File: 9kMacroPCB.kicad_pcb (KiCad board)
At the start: 2 copper layers, 60.3 x 60.3 mm, 25 parts, among them U1 XIAO-RP2040-SMD

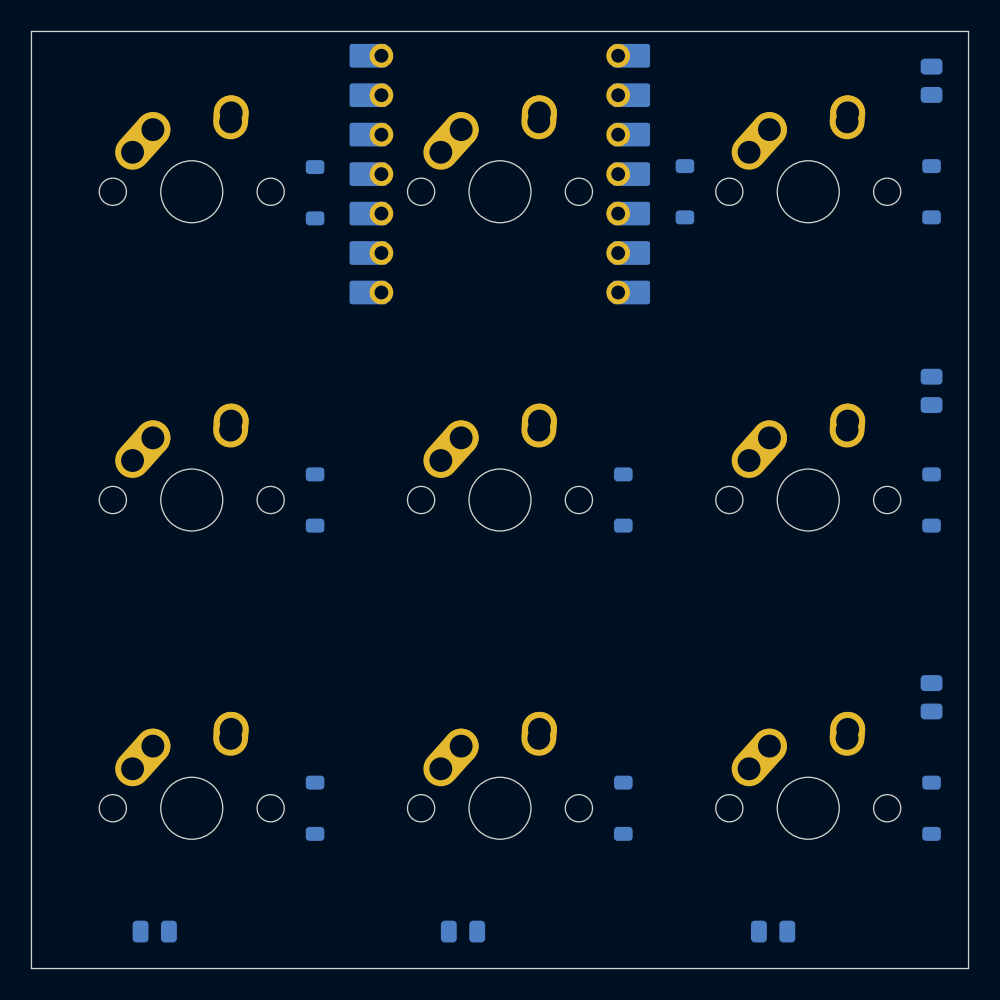
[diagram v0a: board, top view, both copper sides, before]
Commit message: Update PCB: netlist, footprints, and backup cleanup
Removed old backup zip files and added an auto-saved file reference. Updated net assignments and pin naming in 9kMacroPCB.kicad_pcb, made significant changes to footprints (notably D1, R4, and U1), and adjusted component placements and net connections. These changes reflect schematic and layout updates for improved accuracy and maintainability.
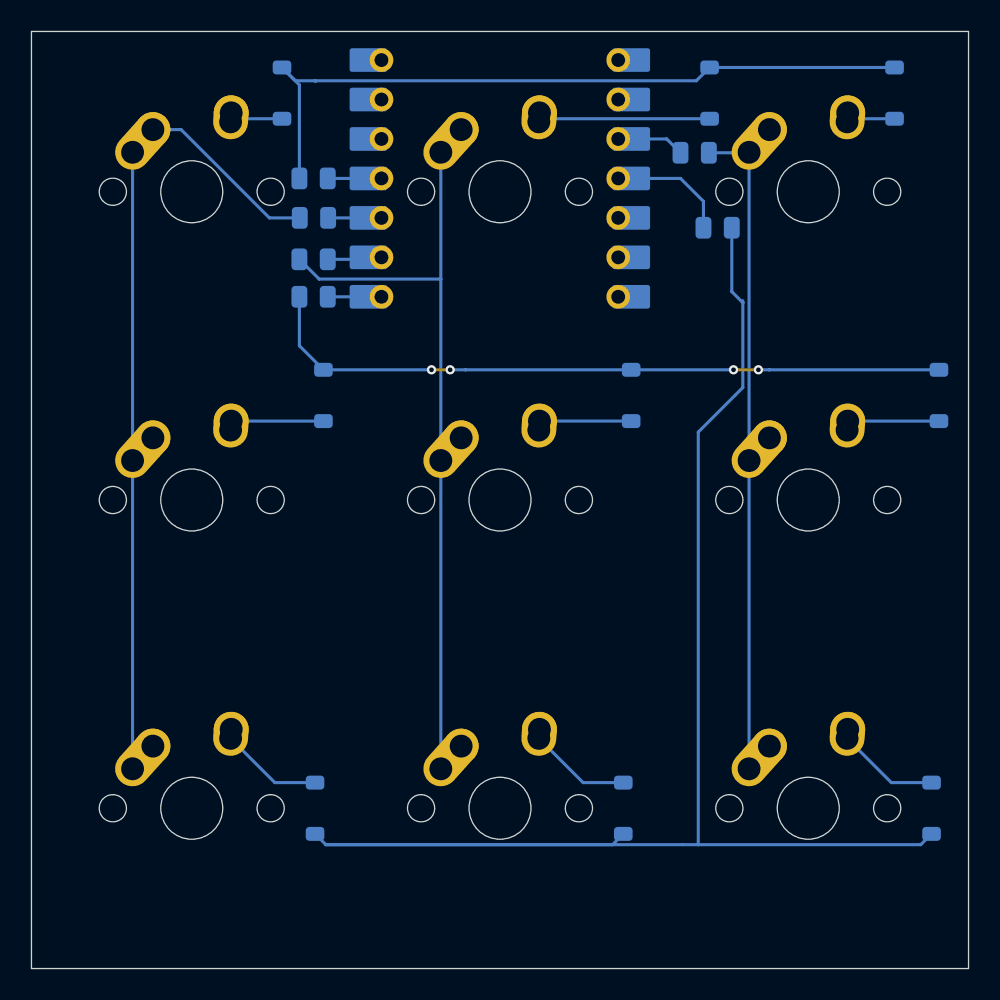
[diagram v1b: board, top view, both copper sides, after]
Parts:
- R1, R2, R3, R4, R5, R6: value 10k -> R_Small
- U1: value XIAO-RP2040-SMD -> XIAO-RP2040-DIP; footprint Seeed Studio XIAO Series Library:XIAO-RP2040-DIP -> XIAO_PCB:XIAO-RP2040-DIP
- moved R5 52.3 mm to (157.0, 47.5)
- moved R3 47.4 mm to (132.5, 56.8), turned to 180 degrees
- moved R6 45.4 mm to (158.5, 52.3)
- moved R4 44.5 mm to (132.5, 54.4)
- moved R2 41.3 mm to (132.5, 51.7), turned to 180 degrees
- moved R1 40.3 mm to (132.5, 49.1), turned to 180 degrees
- moved D3 6.78 mm to (169.9, 43.7), turned to -90 degrees
- moved D1 6.76 mm to (130.4, 43.7), turned to -90 degrees
- moved D4 6.75 mm to (133.1, 63.1), turned to -90 degrees
- moved D5 6.75 mm to (152.9, 63.1), turned to -90 degrees
- moved D6 6.75 mm to (172.7, 63.1), turned to -90 degrees
- moved D2 6.55 mm to (158.0, 43.7), turned to -90 degrees
- moved U1 0.28 mm to (144.5, 49.1)
- renumbered D6 to D2, D7 to D3, D2 to D4, D8 to D6, D3 to D7, D4 to D8
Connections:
- R1 pad 1: unconnected-(R1-Pad1) -> Net-(U1-GPIO3/MOSI)
- R1 pad 2: Net-(U1-GPIO26_A0_D0) -> ROW0
- R2 pad 1: unconnected-(R2-Pad1) -> Net-(U1-GPIO4/MISO)
- R2 pad 2: Net-(U1-GPIO27_A1_D1) -> COL0
- R3 pad 1: unconnected-(R3-Pad1) -> Net-(U1-GPIO1/RX)
- R3 pad 2: Net-(U1-GPIO28_A2_D2) -> ROW1
- R4 pad 1: unconnected-(R4-Pad1) -> Net-(U1-GPIO2/SCK)
- R4 pad 2: Net-(U1-GPIO29_A3_D3) -> COL1
- R5 pad 1: unconnected-(R5-Pad1) -> COL2
- R5 pad 2: Net-(U1-GPIO6_D4_SDA) -> Net-(U1-GPIO28/ADC2/A2)
- R6 pad 1: unconnected-(R6-Pad1) -> ROW2
- R6 pad 2: Net-(U1-GPIO7_D5_SCL) -> Net-(U1-GPIO29/ADC3/A3)
- U1 pad 1: Net-(U1-GPIO26_A0_D0) -> unconnected-(U1-GPIO26/ADC0/A0-Pad1)
- U1 pad 10: unconnected-(U1-GPIO4_D9_MISO-Pad10) -> Net-(U1-GPIO4/MISO)
- U1 pad 11: unconnected-(U1-GPIO3_D10_MOSI-Pad11) -> Net-(U1-GPIO3/MOSI)
- U1 pad 2: Net-(U1-GPIO27_A1_D1) -> unconnected-(U1-GPIO27/ADC1/A1-Pad2)
- U1 pad 3: Net-(U1-GPIO28_A2_D2) -> Net-(U1-GPIO28/ADC2/A2)
- U1 pad 4: Net-(U1-GPIO29_A3_D3) -> Net-(U1-GPIO29/ADC3/A3)
- U1 pad 5: Net-(U1-GPIO6_D4_SDA) -> unconnected-(U1-GPIO6/SDA-Pad5)
- U1 pad 6: Net-(U1-GPIO7_D5_SCL) -> unconnected-(U1-GPIO7/SCL-Pad6)
- U1 pad 8: unconnected-(U1-GPIO1_D7_CSn_RX-Pad8) -> Net-(U1-GPIO1/RX)
- U1 pad 9: unconnected-(U1-GPIO2_D8_SCK-Pad9) -> Net-(U1-GPIO2/SCK)
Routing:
- net ROW2: track 0.00 -> 101.0 mm
- net COL0: track 0.00 -> 51.5 mm
- net COL1: track 0.00 -> 49.3 mm
- net ROW0: track 0.00 -> 47.8 mm
- net ROW1: track 0.00 -> 45.0 mm, vias 0 -> 4
- net COL2: track 0.00 -> 42.3 mm
- net Net-(D2-A): track 0.00 -> 11.1 mm
- net Net-(U1-GPIO29/ADC3/A3): track 0.00 -> 6.96 mm
- net Net-(D9-A): track 0.00 -> 6.62 mm
- net Net-(D8-A): track 0.00 -> 6.62 mm
- net Net-(D7-A): track 0.00 -> 6.62 mm
- net Net-(D4-A): track 0.00 -> 5.94 mm
- net Net-(D5-A): track 0.00 -> 5.91 mm
- net Net-(D6-A): track 0.00 -> 5.87 mm
- net Net-(U1-GPIO28/ADC2/A2): track 0.00 -> 3.54 mm
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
